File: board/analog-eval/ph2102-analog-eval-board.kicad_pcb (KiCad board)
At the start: 2 copper layers, 43.2 x 63.5 mm, 64 parts, among them J1 CONN_PROBE, J2 CONN_OUT, J3 CONN_NTC, U1 LMC662, U2 TLV2333, U3 REF3020, U4 MCP3201-BI/SN, U5 LM27762

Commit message: 改进 layout
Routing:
- net VREF: track 6.46 -> 72.9 mm, vias 0 -> 2
- net +2V5: track 8.68 -> 52.3 mm
- net /NTC_OUT: track 1.45 -> 39.3 mm
- net /VPH: track 4.14 -> 37.7 mm, vias 0 -> 2
- net +3V3: track 13.5 -> 46.9 mm, vias 0 -> 3
- net -2V5: track 4.53 -> 30.5 mm, vias 0 -> 2
- net /ADC_CS: track 2.17 -> 24.6 mm
- net /ADC_MISO: track 0.00 -> 21.9 mm
- net /ADC_SCK: track 0.00 -> 21.4 mm
- net GNDA: track 13.3 -> 17.7 mm, vias 50 -> 51
- net Net-(R15-Pad1): track 0.00 -> 3.25 mm
- net Net-(C6-Pad2): track 23.5 -> 25.2 mm, vias 0 -> 2

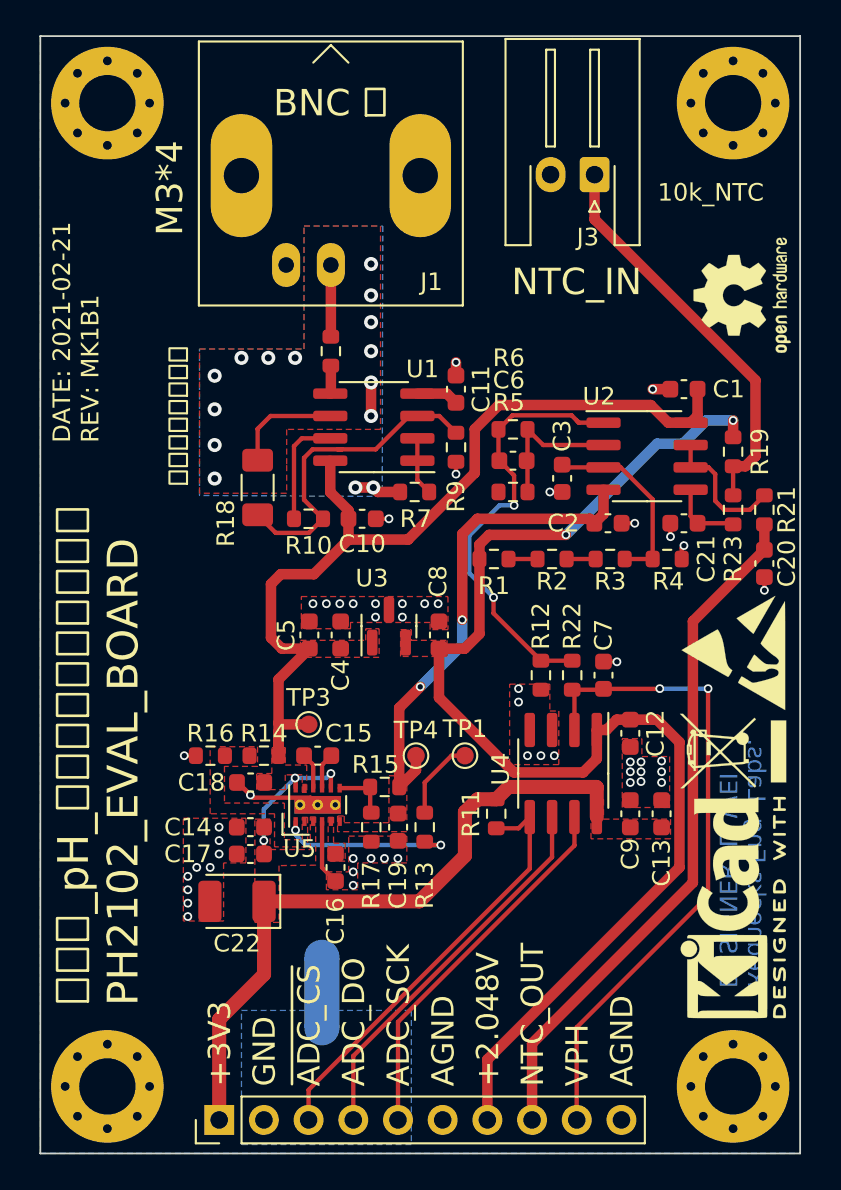
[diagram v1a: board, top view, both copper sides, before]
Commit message: 完善 layout
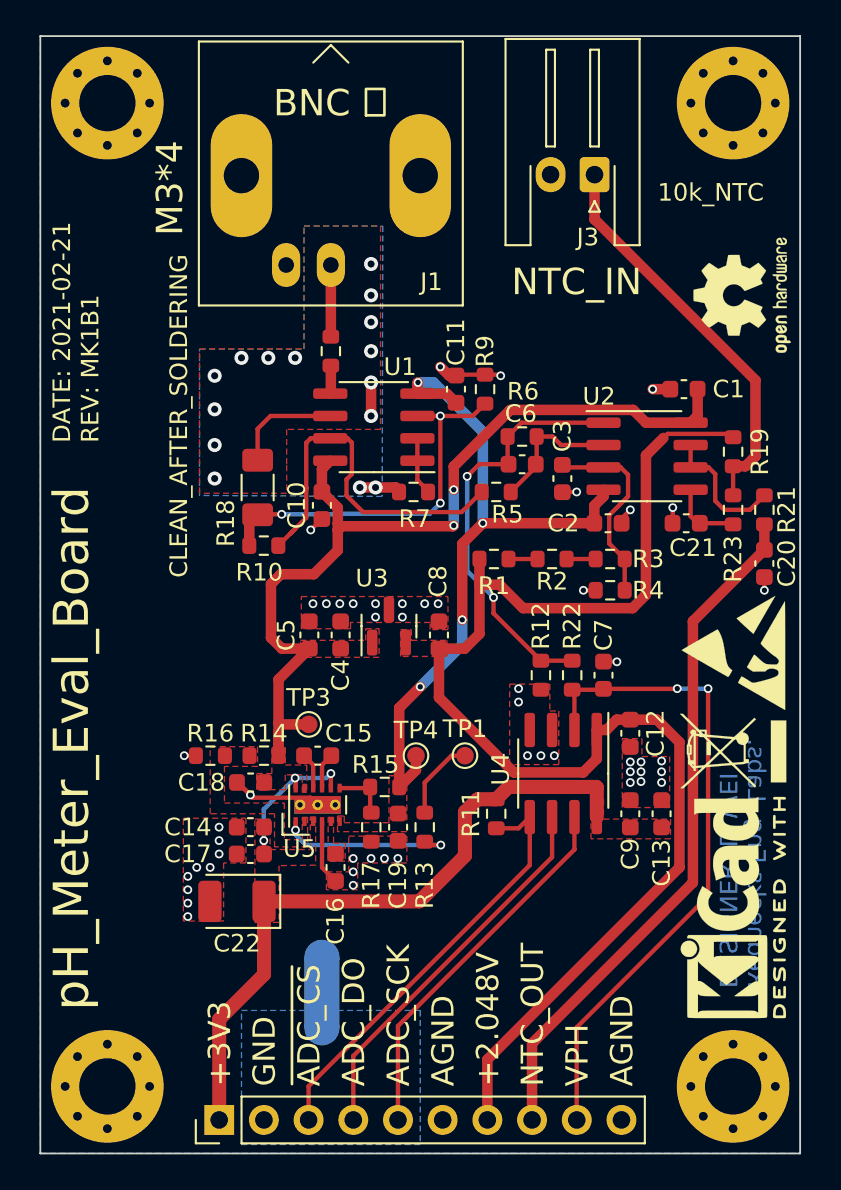
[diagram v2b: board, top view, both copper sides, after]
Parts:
- moved R4 3.69 mm to (33.7, 31.5), turned to 180 degrees
- moved R9 3.69 mm to (26.5, 20.1), turned to 90 degrees
- moved R10 2.96 mm to (14.0, 29.0), turned to 0 degrees
- moved C10 2.41 mm to (17.3, 26.7), turned to 90 degrees
- moved R5 0.95 mm to (27.2, 25.9)
- moved R6 0.66 mm to (28.7, 22.8)
- moved C6 0.56 mm to (28.7, 24.3)
- moved C21 0.13 mm to (38.0, 27.7)
- moved R7 0.06 mm to (22.5, 25.9)
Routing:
- net Net-(R10-Pad2): track 6.37 -> 21.6 mm
- net -2V5: track 30.5 -> 40.7 mm, vias 2 -> 4
- net VREF: track 72.9 -> 77.6 mm, vias 2 -> 0
- net Net-(R10-Pad1): track 18.6 -> 21.9 mm, vias 0 -> 3
- net GNDA: track 17.7 -> 20.4 mm
- net Net-(C6-Pad2): track 25.2 -> 23.9 mm
- net +2V5: track 52.3 -> 52.9 mm, vias 0 -> 2
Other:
- board text added: "${TITLE}"
- board text added: "CLEAN_AFTER_SOLDERING"
- board text removed: "${TITLE} PH2102_EVAL_BOARD"
- board text removed: "保护环焊后需清洁"

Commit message: ready to fabricate
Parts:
- removed TP4: TP_-2V5, TestPoint:TestPoint_Pad_D1.0mm
- R1, R2, R3, R4, R9: value 10k/1% -> 10k/0.1%
- R10: value 9.1k/1% -> 9.1k/0.1%
- R14, R15: value R_Small -> 76.8k
- R16, R17: value R_Small -> 73.2k
- R19: value 10k -> 10k/0.1%
- R5, R6: value 100k -> 10k/0.1%
- R8: value 1M -> 1M/1%
- TP3: value TP_+2V5 -> TP_2V5; footprint TestPoint:TestPoint_Pad_D1.0mm -> Connector_PinHeader_2.54mm:PinHeader_1x02_P2.54mm_Vertical
- moved TP1 2.50 mm to (23.4, 42.4)
- moved TP3 2.08 mm to (17.7, 37.4), turned to 90 degrees
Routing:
- net -2V5: track 40.7 -> 44.4 mm, vias 4 -> 7
- net Net-(R13-Pad1): track 4.63 -> 1.84 mm
- net Net-(R10-Pad2): track 21.6 -> 21.0 mm
- net GNDA: track 20.4 -> 19.9 mm, vias 51 -> 54
- net +2V5: track 52.9 -> 53.4 mm, vias 2 -> 3
- net Net-(R10-Pad1): track 21.9 -> 21.8 mm, vias 3 -> 2
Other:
- board text added: "+2V5"
- board text added: "-2V5"
- board text added: "CLEAN_AFTER SOLDERING"
- board text added: "PGOOD"
- board text removed: "CLEAN_AFTER_SOLDERING"

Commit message: add firmware
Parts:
- removed the REF** at (41.1, 14.7)
- added REF**: OSHW-Logo_7.5x8mm_SilkScreen, Symbol:OSHW-Logo_7.5x8mm_SilkScreen, F.Cu at (39.9, 15.2)
- added kibuzzard-61663736: G***, kibuzzard-61663736, F.Cu at (6.86, 21.7)
- added kibuzzard-6166377A: G***, kibuzzard-6166377A, F.Cu at (11.4, 57.5)
- added kibuzzard-61663788: G***, kibuzzard-61663788, F.Cu at (14.0, 57.5)
- added kibuzzard-616637D2: G***, kibuzzard-616637D2, F.Cu at (16.5, 55.6)
- added kibuzzard-616637F4: G***, kibuzzard-616637F4, F.Cu at (19.1, 55.6)
- added kibuzzard-61663800: G***, kibuzzard-61663800, F.Cu at (21.6, 55.0)
- added kibuzzard-6166380D: G***, kibuzzard-6166380D, F.Cu at (34.3, 56.9)
- added kibuzzard-6166380D: G***, kibuzzard-6166380D, F.Cu at (24.1, 56.9)
- added kibuzzard-6166382A: G***, kibuzzard-6166382A, F.Cu at (26.7, 56.9)
- added kibuzzard-61663837: G***, kibuzzard-61663837, F.Cu at (29.2, 55.1)
- added kibuzzard-61663842: G***, kibuzzard-61663842, F.Cu at (31.8, 57.5)
- added kibuzzard-6166390D: G***, kibuzzard-6166390D, F.Cu at (8.74, 9.91)
- added kibuzzard-61663968: G***, kibuzzard-61663968, F.Cu at (30.3, 12.8)
- added kibuzzard-61663979: G***, kibuzzard-61663979, F.Cu at (32.8, 12.8)
- added kibuzzard-61663E77: G***, kibuzzard-61663E77, F.Cu at (13.3, 37.4)
- added kibuzzard-61663E8D: G***, kibuzzard-61663E8D, F.Cu at (24.4, 37.4)
- added kibuzzard-61670BF9: G***, kibuzzard-61670BF9, F.Cu at (3.51, 31.9)
- moved R18 3.31 mm to (14.8, 22.6)
- moved R10 3.23 mm to (14.4, 25.8)
- moved TP1 1.36 mm to (23.1, 41.1)
- moved R11 0.68 mm to (27.4, 43.6)
- moved J3 0.61 mm to (32.8, 8.48)
- moved C12 0.58 mm to (34.8, 40.2)
- moved R16 0.23 mm to (11.0, 40.7)
- moved C15 0.23 mm to (17.0, 40.7)
- moved R14 0.23 mm to (14.0, 40.7)
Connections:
- J2 pad 8: /NTC_OUT -> /VPH
- J2 pad 9: /VPH -> /NTC_OUT
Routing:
- net +2V5: track 53.4 -> 46.5 mm, vias 3 -> 4
- net Net-(R10-Pad2): track 21.0 -> 17.7 mm
- net Net-(R18-Pad2): track 6.21 -> 3.19 mm
- net /NTC_IN: track 22.9 -> 24.8 mm
- net Net-(R10-Pad1): track 21.8 -> 23.4 mm
- net Net-(R13-Pad1): track 1.84 -> 3.04 mm
- net /GUARD: track 4.30 -> 5.45 mm, vias 15 -> 22
- net /VPH: track 37.4 -> 36.5 mm, vias 2 -> 0
- net VREF: track 77.3 -> 76.6 mm
- net /ADC_CS: track 24.6 -> 24.1 mm
- net GNDA: track 19.9 -> 19.8 mm, vias 54 -> 217
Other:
- board text added: "BNC"
- board text added: "JLCJLCJLCJLC"
- board text removed: "${TITLE}"
- board text removed: "+2.048V"
- board text removed: "+2V5"
- board text removed: "+3V3"
- board text removed: "-2V5"
- board text removed: "ADC_DO"
- board text removed: "ADC_SCK"
- board text removed: "AGND"
- board text removed: "BNC 座"
- board text removed: "GND"
- board text removed: "M3*4"
- board text removed: "NTC_IN"
- board text removed: "NTC_OUT"
- board text removed: "VPH"
- board text removed: "~ADC_CS"
